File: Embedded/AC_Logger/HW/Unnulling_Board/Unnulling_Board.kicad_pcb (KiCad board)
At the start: 2 copper layers, 58.4 x 50.8 mm, 9 parts, among them J1 Screw_Terminal_01x03, J2 Screw_Terminal_01x04, K1 RT424730, K2 RT424730

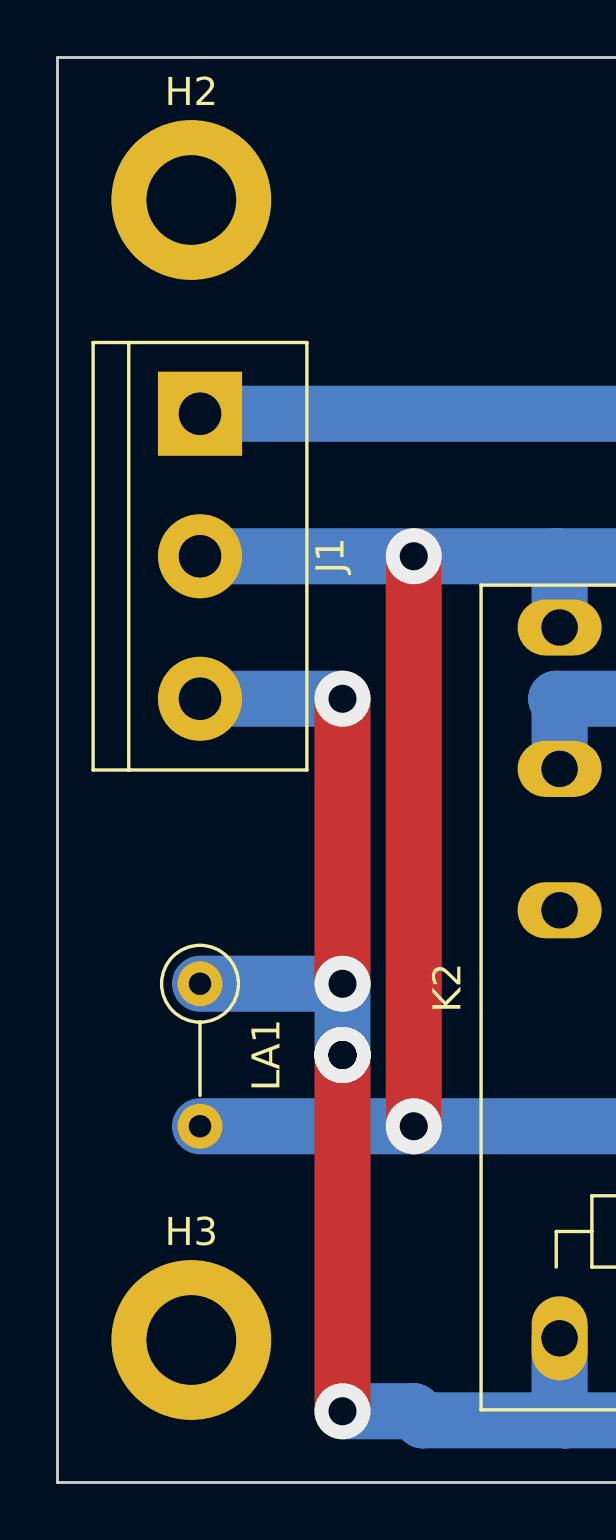
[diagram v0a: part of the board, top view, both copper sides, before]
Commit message: PCB changed to make sandwitch.
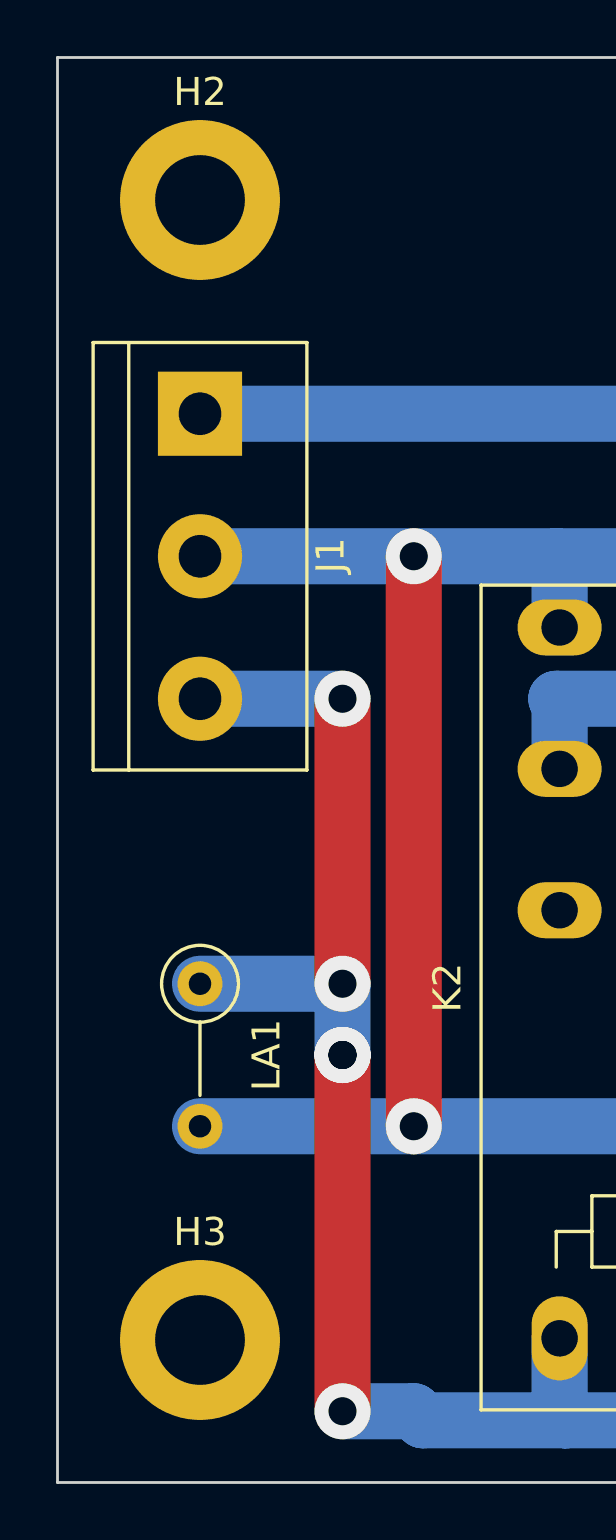
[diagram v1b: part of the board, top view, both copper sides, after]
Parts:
- moved H2 0.31 mm to (48.3, 40.6)
- moved H3 0.31 mm to (48.3, 81.3)
